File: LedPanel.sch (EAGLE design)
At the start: 12 parts, among them U1 AL8805W5-7

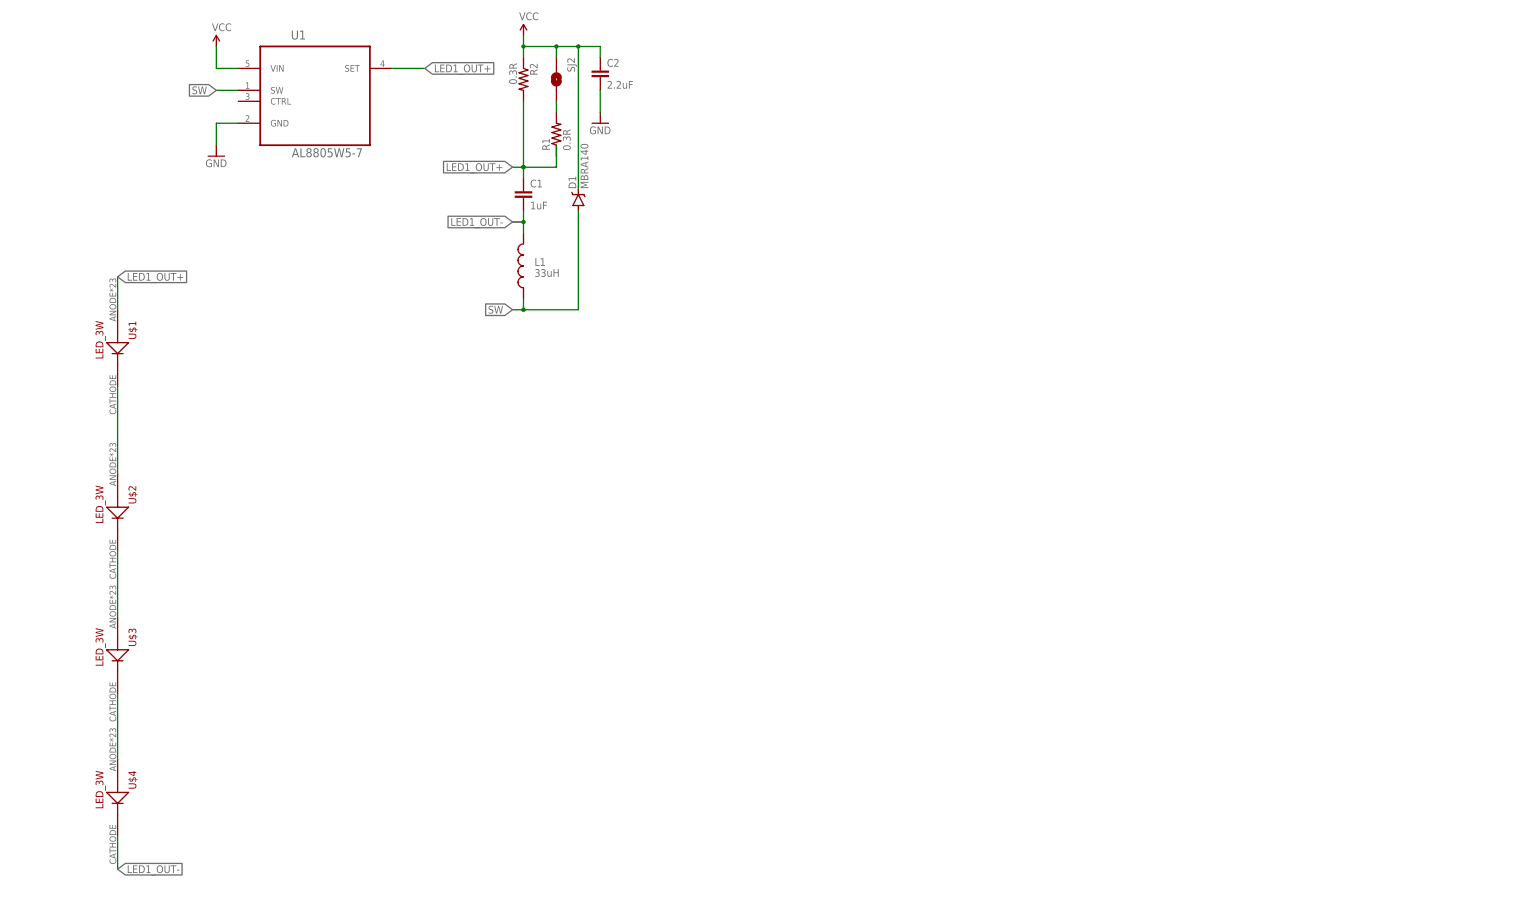
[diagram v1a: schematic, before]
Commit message: Creating 3 string of 4 leds. 12 3W leds in total. Peak power is 36W?
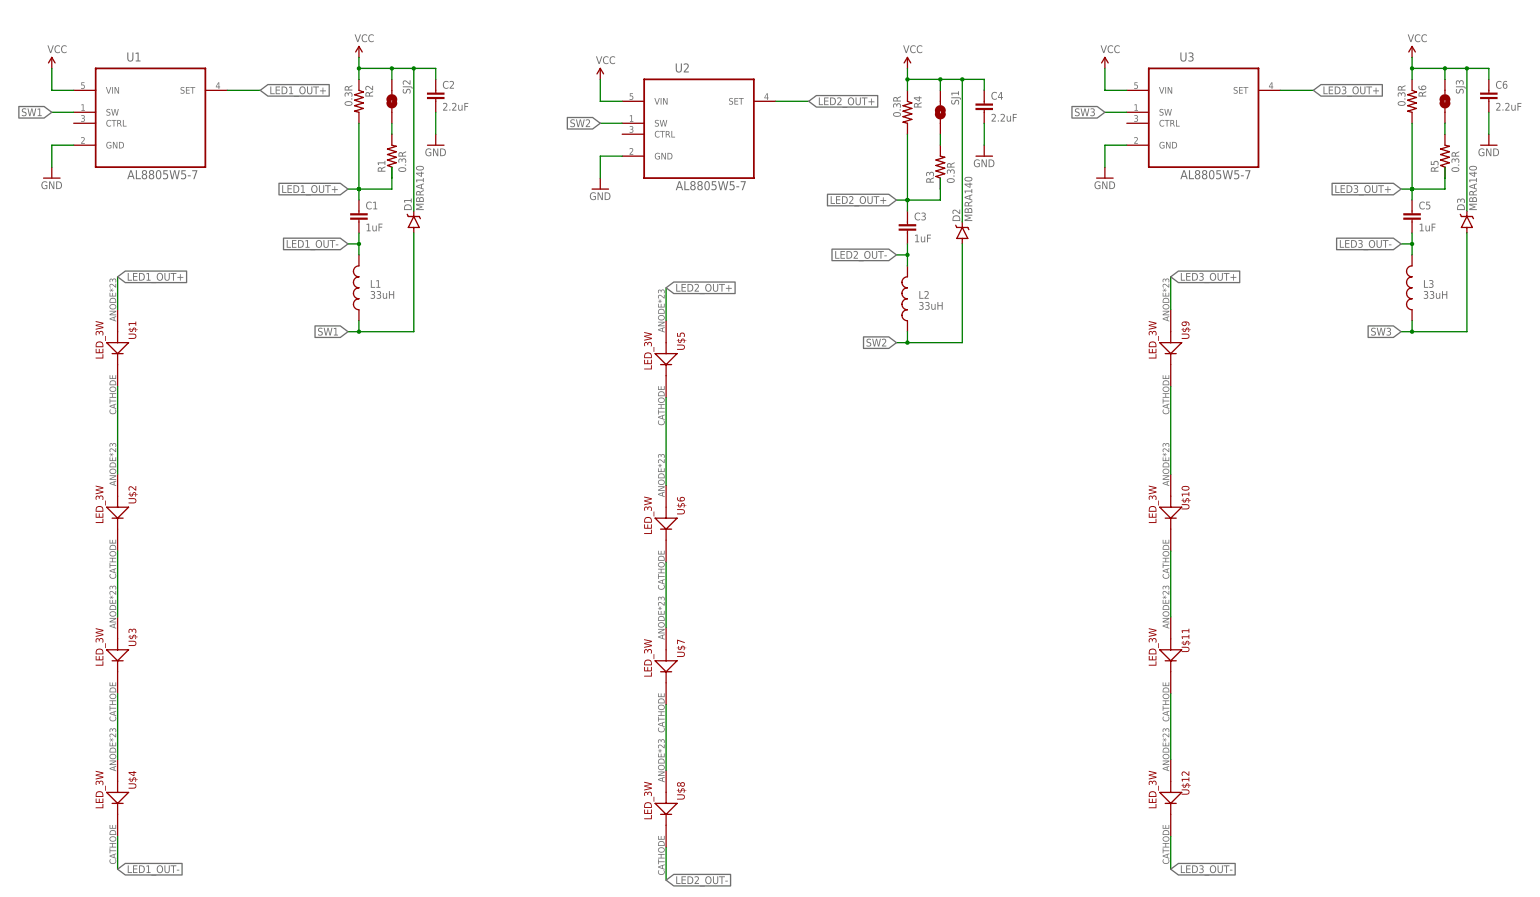
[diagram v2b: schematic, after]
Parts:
- added C3, C5: 1uF, SparkFun-Capacitors:1.0UF50V10%(1206)
- added C4, C6: 2.2uF, SparkFun-Capacitors:2.2UF50V10%(1206)
- added D2, D3: MBRA140, SparkFun-DiscreteSemi:DIODE-SCHOTTKY-MBRA140
- added L2, L3: 33uH, SparkFun-Passives:INDUCTORBOURNS_SRN6045
- added R3, R4, R5, R6: 0.3R, SparkFun-Resistors:0.3OHM-1/8W-1%(0805)
- added SJ1, SJ3: NO Jumper, SparkFun-Passives:JUMPER-PAD-2-NO
- added U$10, U$11, U$12, U$5, U$6, U$7, U$8, U$9: LED_3W, LedPanel:LED_3W
- added U2, U3: AL8805W5-7, LedPanel:AL8805W5-7
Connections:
- net SW renamed SW1
- new net LED2_OUT+: C3.1, R3.1, R4.2, U$5.ANODE, U2.SET
- new net LED2_OUT-: C3.2, L2.2, U$8.CATHODE
- new net LED3_OUT+: C5.1, R5.1, R6.2, U$9.ANODE, U3.SET
- new net LED3_OUT-: C5.2, L3.2, U$12.CATHODE
- new net N$10: U$10.CATHODE, U$11.ANODE
- new net N$11: U$10.ANODE, U$9.CATHODE
- new net N$12: R5.2, SJ3.2
- new net N$4: U$7.CATHODE, U$8.ANODE
- new net N$5: U$6.CATHODE, U$7.ANODE
- new net N$7: U$5.CATHODE, U$6.ANODE
- new net N$8: R3.2, SJ1.2
- new net N$9: U$11.CATHODE, U$12.ANODE
- new net SW2: D2.A, L2.1, U2.SW
- new net SW3: D3.A, L3.1, U3.SW
- net GND: now also C4.2, C6.2, U2.GND, U3.GND
- net VCC: now also C4.1, C6.1, D2.C, D3.C, R4.1, R6.1, SJ1.1, SJ3.1, U2.VIN, U3.VIN
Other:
- moved on the sheet: C1, C2, D1, L1, R1, R2, SJ2, U1

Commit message: Adding ws8211 to control the leds
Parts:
- added 5V, U$16: 5V, LedPanel:SOLDER_PAD
- added DI: DI, LedPanel:SOLDER_PAD
- added DO: DO, LedPanel:SOLDER_PAD
- added IC1: WS2811-SOP8, LedPanel:WS2811-SOP8
- added R7, R8, R9: 4.7k, SparkFun-Resistors:0.3OHM-1/8W-1%(0805)
- added U$15, U$18: GND, LedPanel:SOLDER_PAD
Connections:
- new net 5V: 5V.P$1, IC1.VDD, R7.1, R8.1, R9.1, U$16.P$1
- new net CTRL1: IC1.R, R7.2, U1.CTRL
- new net CTRL2: IC1.G, R8.2, U2.CTRL
- new net CTRL3: IC1.B, R9.2, U3.CTRL
- new net N$13: DI.P$1, IC1.DIN
- new net N$14: DO.P$1, IC1.DO
- net GND: now also IC1.GND, U$15.P$1, U$18.P$1
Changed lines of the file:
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@@
 <part name="SJ3" library="SparkFun-Passives" deviceset="JUMPER-PAD-2-NO" device="" value="NO Jumper"/>
 <part name="P+6" library="LedPanel" deviceset="VCC" device=""/>
+<part name="IC1" library="LedPanel" deviceset="WS2811" device="-SOP8"/>
+<part name="GND6" library="LedPanel" deviceset="GND" device=""/>
+<part name="SUPPLY1" library="LedPanel" deviceset="5V" device=""/>
+<part name="R7" library="SparkFun-Resistors" deviceset="0.3OHM-1/8W-1%(0805)" device="" value="4.7k"/>
+<part name="R8" library="SparkFun-Resistors" deviceset="0.3OHM-1/8W-1%(0805)" device="" value="4.7k"/>
+<part name="R9" library="SparkFun-Resistors" deviceset="0.3OHM-1/8W-1%(0805)" device="" value="4.7k"/>
+<part name="SUPPLY2" library="LedPanel" deviceset="5V" device=""/>
+<part name="5V" library="LedPanel" deviceset="SOLDER_PAD" device="" value="5V"/>
+<part name="DI" library="LedPanel" deviceset="SOLDER_PAD" device="" value="DI"/>
+<part name="U$15" library="LedPanel" deviceset="SOLDER_PAD" device="" value="GND"/>
+<part name="U$16" library="LedPanel" deviceset="SOLDER_PAD" device="" value="5V"/>
+<part name="DO" library="LedPanel" deviceset="SOLDER_PAD" device="" value="DO"/>
+<part name="U$18" library="LedPanel" deviceset="SOLDER_PAD" device="" value="GND"/>
+<part name="SUPPLY3" library="LedPanel" deviceset="5V" device=""/>
+<part name="GND7" library="LedPanel" deviceset="GND" device=""/>
 </parts>
 <sheets>
@@
 </instance>
 <instance part="P+6" gate="1" x="330.2" y="139.7"/>
+<instance part="IC1" gate="G$1" x="165.1" y="190.5"/>
+<instance part="GND6" gate="1" x="149.86" y="182.88"/>
+<instance part="SUPPLY1" gate="G$1" x="182.88" y="200.66"/>
+<instance part="R7" gate="G$1" x="132.08" y="208.28" rot="R270"/>
+<instance part="R8" gate="G$1" x="119.38" y="208.28" rot="R270"/>
+<instance part="R9" gate="G$1" x="106.68" y="208.28" rot="R270"/>
+<instance part="SUPPLY2" gate="G$1" x="119.38" y="218.44"/>
+<instance part="5V" gate="A" x="162.56" y="233.68" rot="R270"/>
+<instance part="DI" gate="A" x="187.96" y="190.5" rot="R90"/>
+<instance part="U$15" gate="A" x="162.56" y="228.6" rot="R270"/>
+<instance part="U$16" gate="A" x="177.8" y="233.68" rot="R90"/>
+<instance part="DO" gate="A" x="193.04" y="187.96" rot="R90"/>
+<instance part="U$18" gate="A" x="177.8" y="228.6" rot="R90"/>
+<instance part="SUPPLY3" gate="G$1" x="170.18" y="233.68"/>
+<instance part="GND7" gate="1" x="170.18" y="226.06"/>
 </instances>
 <busses>
@@
 <pinref part="GND5" gate="1" pin="GND"/>
 </segment>
+<segment>
+<pinref part="IC1" gate="G$1" pin="GND"/>
+<pinref part="GND6" gate="1" pin="GND"/>
+<wire x1="152.4" y1="187.96" x2="149.86" y2="187.96" width="0.1524" layer="91"/>
+<wire x1="149.86" y1="187.96" x2="149.86" y2="185.42" width="0.1524" layer="91"/>
+</segment>
+<segment>
+<pinref part="U$15" gate="A" pin="P$1"/>
+<pinref part="GND7" gate="1" pin="GND"/>
+<wire x1="167.64" y1="228.6" x2="170.18" y2="228.6" width="0.1524" layer="91"/>
+<pinref part="U$18" gate="A" pin="P$1"/>
+<wire x1="170.18" y1="228.6" x2="172.72" y2="228.6" width="0.1524" layer="91"/>
+<junction x="170.18" y="228.6"/>
+</segment>
 </net>
 <net name="LED1_OUT-" class="1">
@@
 </segment>
 </net>
+<net name="5V" class="0">
+<segment>
+<pinref part="IC1" gate="G$1" pin="VDD"/>
+<pinref part="SUPPLY1" gate="G$1" pin="5V"/>
+<wire x1="177.8" y1="195.58" x2="182.88" y2="195.58" width="0.1524" layer="91"/>
+<wire x1="182.88" y1="195.58" x2="182.88" y2="200.66" width="0.1524" layer="91"/>
+</segment>
+<segment>
+<pinref part="R9" gate="G$1" pin="1"/>
+<wire x1="106.68" y1="213.36" x2="106.68" y2="215.9" width="0.1524" layer="91"/>
+<pinref part="R7" gate="G$1" pin="1"/>
+<wire x1="106.68" y1="215.9" x2="119.38" y2="215.9" width="0.1524" layer="91"/>
+<wire x1="119.38" y1="215.9" x2="132.08" y2="215.9" width="0.1524" layer="91"/>
+<wire x1="132.08" y1="215.9" x2="132.08" y2="213.36" width="0.1524" layer="91"/>
+<pinref part="R8" gate="G$1" pin="1"/>
+<wire x1="119.38" y1="213.36" x2="119.38" y2="215.9" width="0.1524" layer="91"/>
+<pinref part="SUPPLY2" gate="G$1" pin="5V"/>
+<wire x1="119.38" y1="218.44" x2="119.38" y2="215.9" width="0.1524" layer="91"/>
+<junction x="119.38" y="215.9"/>
+</segment>
+<segment>
+<pinref part="U$16" gate="A" pin="P$1"/>
+<pinref part="SUPPLY3" gate="G$1" pin="5V"/>
+<wire x1="172.72" y1="233.68" x2="170.18" y2="233.68" width="0.1524" layer="91"/>
+<pinref part="5V" gate="A" pin="P$1"/>
+<wire x1="170.18" y1="233.68" x2="167.64" y2="233.68" width="0.1524" layer="91"/>
+<junction x="170.18" y="233.68"/>
+</segment>
+</net>
+<net name="CTRL1" class="0">
+<segment>
+<pinref part="IC1" gate="G$1" pin="R"/>
+<pinref part="R7" gate="G$1" pin="2"/>
+<wire x1="152.4" y1="195.58" x2="132.08" y2="195.58" width="0.1524" layer="91"/>
+<wire x1="132.08" y1="195.58" x2="132.08" y2="203.2" width="0.1524" layer="91"/>
+<label x="132.08" y="195.58" size="1.778" layer="95" rot="R180" xref="yes"/>
+</segment>
+<segment>
+<pinref part="U1" gate="A" pin="CTRL"/>
+<wire x1="20.32" y1="124.46" x2="7.62" y2="124.46" width="0.1524" layer="91"/>
+<label x="7.62" y="124.46" size="1.778" layer="95" rot="R180" xref="yes"/>
+</segment>
+</net>
+<net name="CTRL2" class="0">
+<segment>
+<pinref part="IC1" gate="G$1" pin="G"/>
+<pinref part="R8" gate="G$1" pin="2"/>
+<wire x1="152.4" y1="193.04" x2="119.38" y2="193.04" width="0.1524" layer="91"/>
+<wire x1="119.38" y1="193.04" x2="119.38" y2="203.2" width="0.1524" layer="91"/>
+<label x="119.38" y="193.04" size="1.778" layer="95" rot="R180" xref="yes"/>
+</segment>
+<segment>
+<pinref part="U2" gate="A" pin="CTRL"/>
+<wire x1="147.32" y1="121.92" x2="134.62" y2="121.92" width="0.1524" layer="91"/>
+<label x="134.62" y="121.92" size="1.778" layer="95" rot="R180" xref="yes"/>
+</segment>
+</net>
+<net name="CTRL3" class="0">
+<segment>
+<pinref part="IC1" gate="G$1" pin="B"/>
+<pinref part="R9" gate="G$1" pin="2"/>
+<wire x1="152.4" y1="190.5" x2="106.68" y2="190.5" width="0.1524" layer="91"/>
+<wire x1="106.68" y1="190.5" x2="106.68" y2="203.2" width="0.1524" layer="91"/>
+<label x="106.68" y="190.5" size="1.778" layer="95" rot="R180" xref="yes"/>
+</segment>
+<segment>
+<pinref part="U3" gate="A" pin="CTRL"/>
+<wire x1="264.16" y1="124.46" x2="251.46" y2="124.46" width="0.1524" layer="91"/>
+<label x="251.46" y="124.46" size="1.778" layer="95" rot="R180" xref="yes"/>
+</segment>
+</net>
+<net name="N$13" class="0">
+<segment>
+<pinref part="DI" gate="A" pin="P$1"/>
+<pinref part="IC1" gate="G$1" pin="DIN"/>
+<wire x1="182.88" y1="190.5" x2="177.8" y2="190.5" width="0.1524" layer="91"/>
+<junction x="177.8" y="190.5"/>
+</segment>
+</net>
+<net name="N$14" class="0">
+<segment>
+<pinref part="DO" gate="A" pin="P$1"/>
+<wire x1="187.96" y1="187.96" x2="177.8" y2="187.96" width="0.1524" layer="91"/>
+<pinref part="IC1" gate="G$1" pin="DO"/>
+<junction x="177.8" y="187.96"/>
+</segment>
+</net>

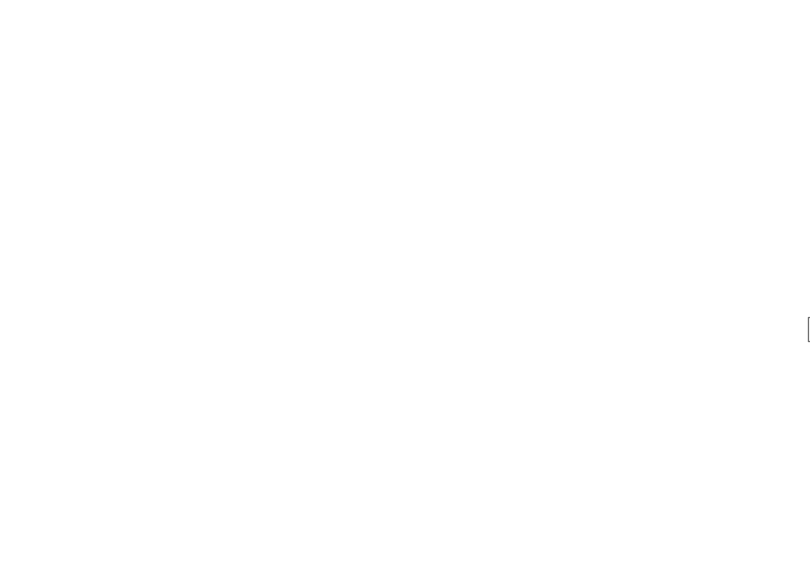
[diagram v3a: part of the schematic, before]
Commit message: Layout first led driver
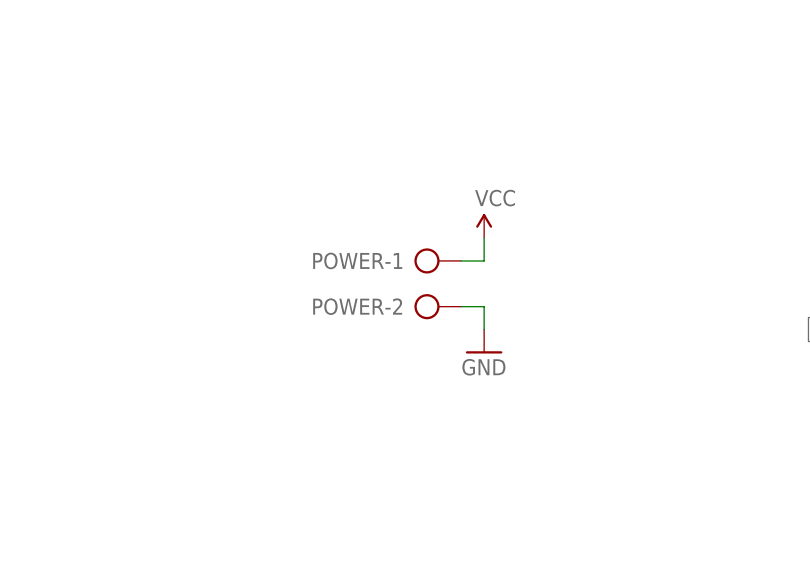
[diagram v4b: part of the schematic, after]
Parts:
- added POWER: (no value), LedPanel:AK500/2
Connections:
- net GND: now also POWER-2.KL
- net VCC: now also POWER-1.KL
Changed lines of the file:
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@@
 </variantdefs>
 <classes>
-<class number="0" name="default" width="0.254" drill="0">
+<class number="0" name="default" width="0.1524" drill="0.3048">
+<clearance class="0" value="0.1524"/>
 </class>
-<class number="1" name="power" width="0.508" drill="0">
+<class number="1" name="power" width="0.1524" drill="0.3048">
+<clearance class="1" value="0.1524"/>
 </class>
 </classes>
@@
 <part name="SUPPLY3" library="LedPanel" deviceset="5V" device=""/>
 <part name="GND7" library="LedPanel" deviceset="GND" device=""/>
+<part name="POWER" library="LedPanel" deviceset="AK500/2" device=""/>
+<part name="P+7" library="LedPanel" deviceset="VCC" device=""/>
+<part name="GND8" library="LedPanel" deviceset="GND" device=""/>
 </parts>
 <sheets>
@@
 <instance part="SUPPLY3" gate="G$1" x="170.18" y="233.68"/>
 <instance part="GND7" gate="1" x="170.18" y="226.06"/>
+<instance part="POWER" gate="-1" x="53.34" y="198.12"/>
+<instance part="POWER" gate="-2" x="53.34" y="193.04"/>
+<instance part="P+7" gate="1" x="60.96" y="200.66"/>
+<instance part="GND8" gate="1" x="60.96" y="187.96"/>
 </instances>
 <busses>
@@
 <pinref part="P+6" gate="1" pin="VCC"/>
 </segment>
+<segment>
+<pinref part="POWER" gate="-1" pin="KL"/>
+<pinref part="P+7" gate="1" pin="VCC"/>
+<wire x1="58.42" y1="198.12" x2="60.96" y2="198.12" width="0.1524" layer="91"/>
+<wire x1="60.96" y1="198.12" x2="60.96" y2="200.66" width="0.1524" layer="91"/>
+</segment>
 </net>
 <net name="GND" class="0">
@@
 <wire x1="170.18" y1="228.6" x2="172.72" y2="228.6" width="0.1524" layer="91"/>
 <junction x="170.18" y="228.6"/>
+</segment>
+<segment>
+<pinref part="POWER" gate="-2" pin="KL"/>
+<pinref part="GND8" gate="1" pin="GND"/>
+<wire x1="58.42" y1="193.04" x2="60.96" y2="193.04" width="0.1524" layer="91"/>
+<wire x1="60.96" y1="193.04" x2="60.96" y2="190.5" width="0.1524" layer="91"/>
 </segment>
 </net>
@@
 <net name="CTRL1" class="0">
 <segment>
+<pinref part="U1" gate="A" pin="CTRL"/>
+<wire x1="20.32" y1="124.46" x2="7.62" y2="124.46" width="0.1524" layer="91"/>
+<label x="7.62" y="124.46" size="1.778" layer="95" rot="R180" xref="yes"/>
+</segment>
+<segment>
 <pinref part="IC1" gate="G$1" pin="R"/>
 <pinref part="R7" gate="G$1" pin="2"/>
@@
 <label x="132.08" y="195.58" size="1.778" layer="95" rot="R180" xref="yes"/>
 </segment>
-<segment>
-<pinref part="U1" gate="A" pin="CTRL"/>
-<wire x1="20.32" y1="124.46" x2="7.62" y2="124.46" width="0.1524" layer="91"/>
-<label x="7.62" y="124.46" size="1.778" layer="95" rot="R180" xref="yes"/>
-</segment>
 </net>
 <net name="CTRL2" class="0">
@@
 <net name="CTRL3" class="0">
 <segment>
+<pinref part="U3" gate="A" pin="CTRL"/>
+<wire x1="264.16" y1="124.46" x2="251.46" y2="124.46" width="0.1524" layer="91"/>
+<label x="251.46" y="124.46" size="1.778" layer="95" rot="R180" xref="yes"/>
+</segment>
+<segment>
 <pinref part="IC1" gate="G$1" pin="B"/>
 <pinref part="R9" gate="G$1" pin="2"/>
@@
 <label x="106.68" y="190.5" size="1.778" layer="95" rot="R180" xref="yes"/>
 </segment>
-<segment>
-<pinref part="U3" gate="A" pin="CTRL"/>
-<wire x1="264.16" y1="124.46" x2="251.46" y2="124.46" width="0.1524" layer="91"/>
-<label x="251.46" y="124.46" size="1.778" layer="95" rot="R180" xref="yes"/>
-</segment>
-</net>
+</net>
